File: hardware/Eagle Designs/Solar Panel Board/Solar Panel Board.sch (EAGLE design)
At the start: 34 parts, among them J1 MOLEX_503763-0291MOLEX_503763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, J2 MOLEX_503763-0491MOLEX_503763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

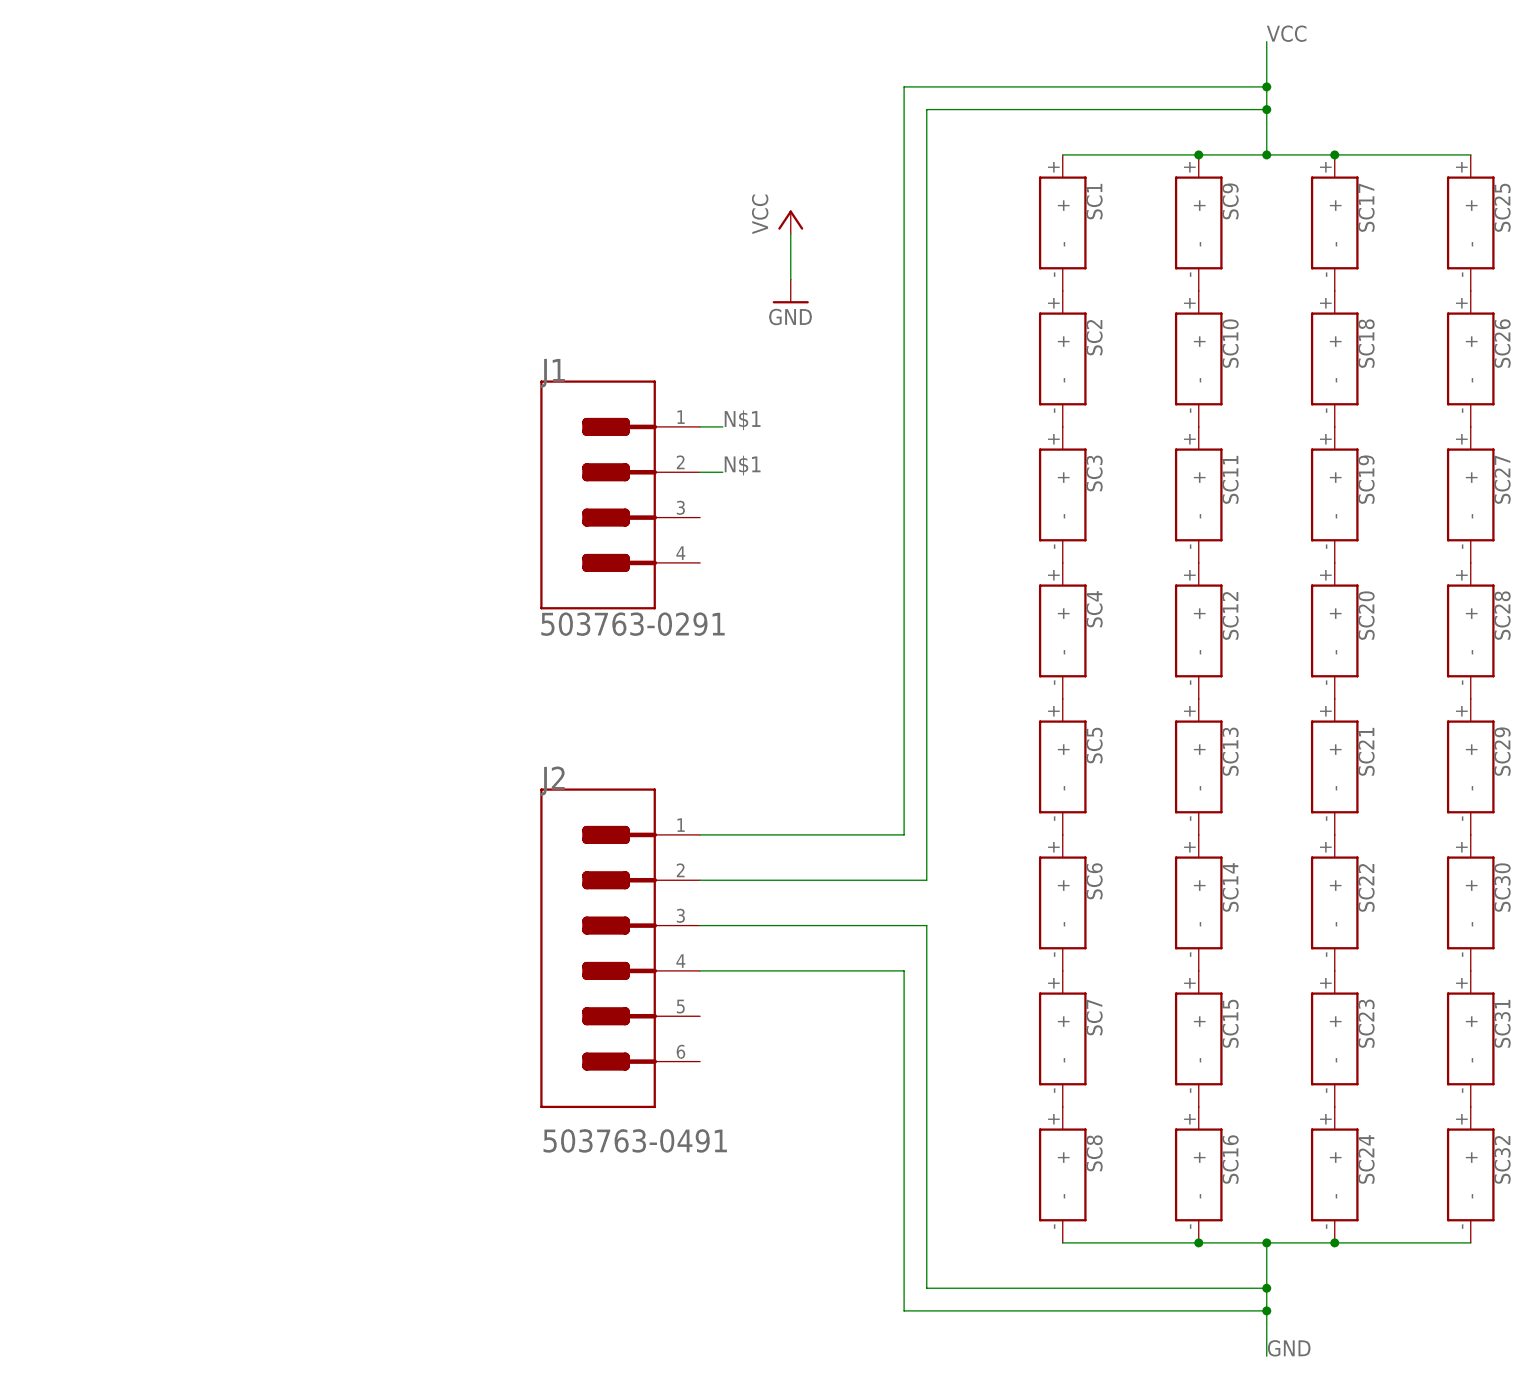
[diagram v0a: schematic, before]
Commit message: Moved solar panel boards to Eagle folder, deleted redudant OBC files
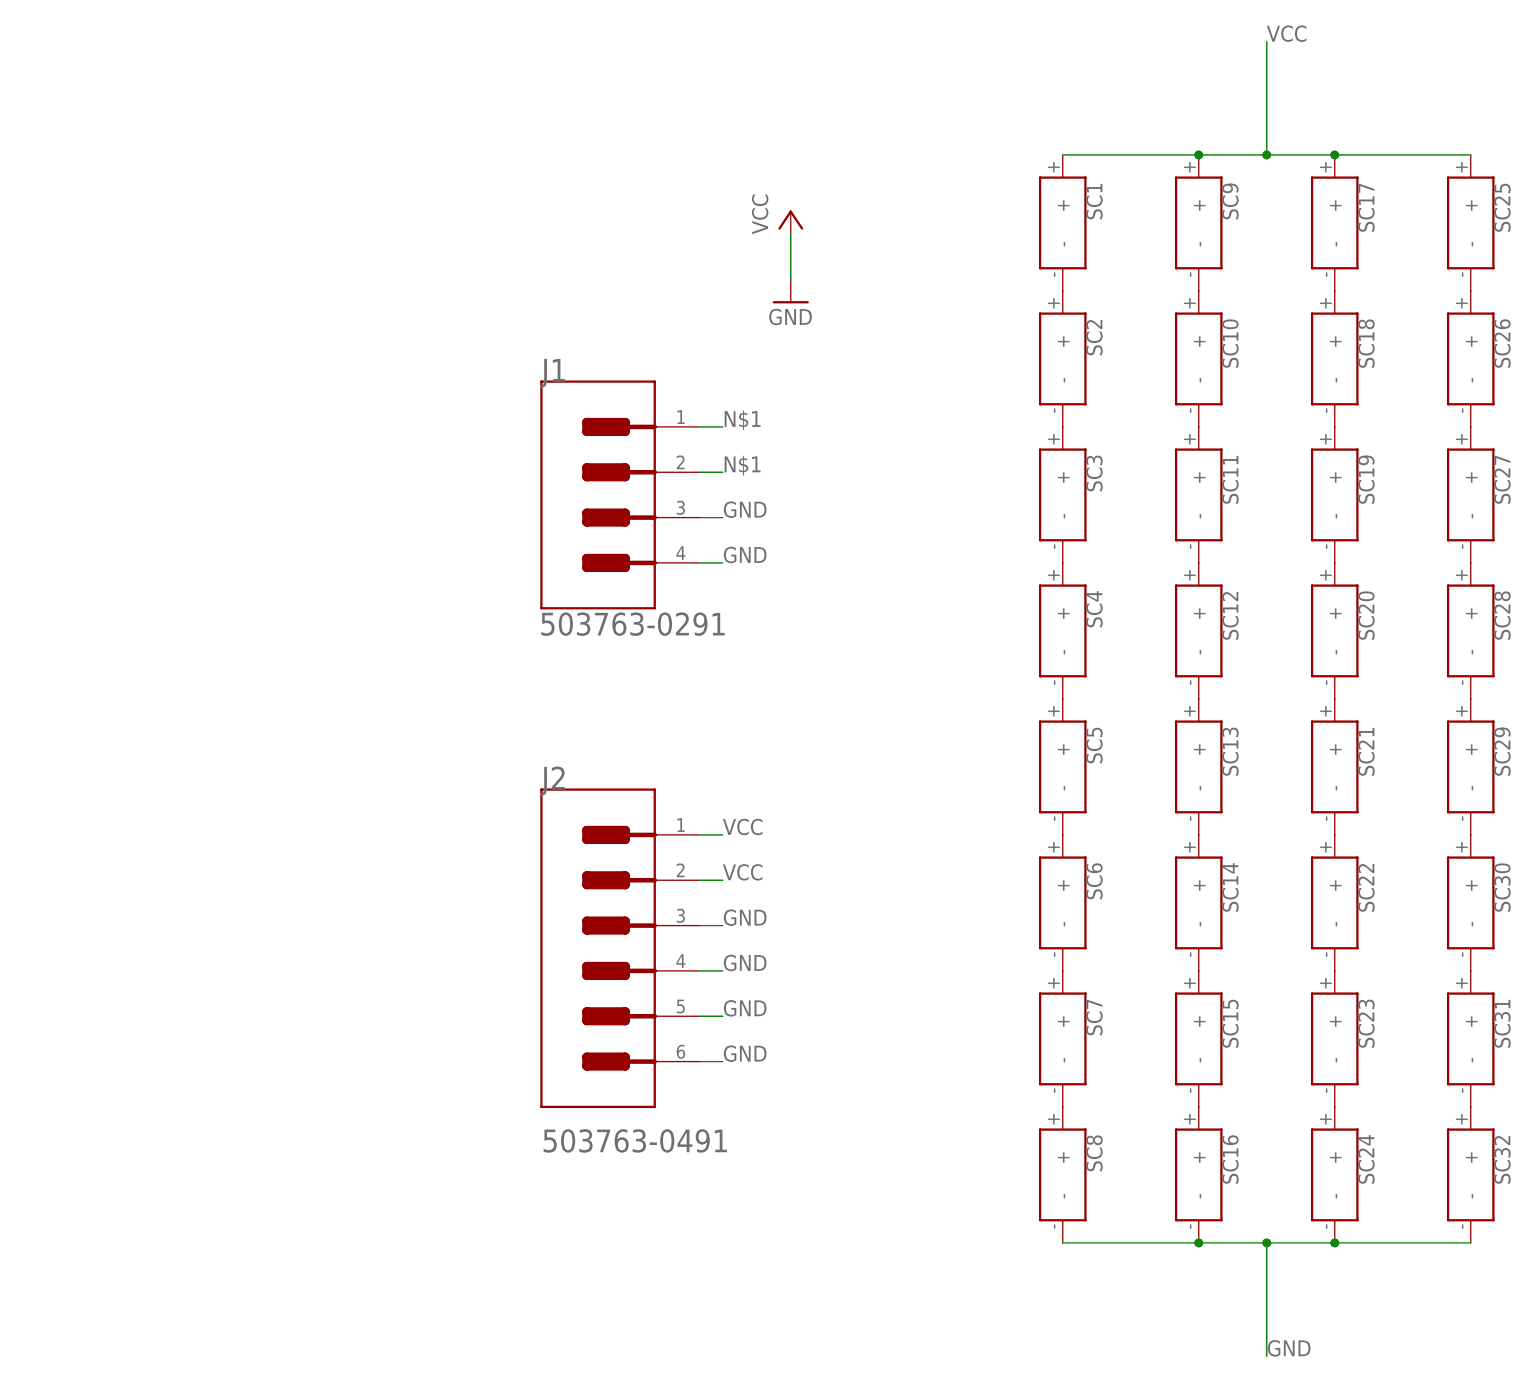
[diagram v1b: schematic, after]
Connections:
- net GND: now also J1.MNT_1, J1.MNT_2, J2.MNT_1, J2.MNT_2
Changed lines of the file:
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@@
 <segment>
 <pinref part="J2" gate="G$0" pin="1"/>
-<wire x1="416.56" y1="-33.02" x2="439.42" y2="-33.02" width="0.1524" layer="91"/>
-<wire x1="439.42" y1="-33.02" x2="439.42" y2="50.8" width="0.1524" layer="91"/>
+<wire x1="416.56" y1="-33.02" x2="419.1" y2="-33.02" width="0.1524" layer="91"/>
+<label x="419.1" y="-33.02" size="1.778" layer="95"/>
+</segment>
+<segment>
 <pinref part="SC25" gate="G$1" pin="+"/>
 <pinref part="SC17" gate="G$1" pin="+"/>
@@
 <junction x="487.68" y="43.18"/>
 <wire x1="480.06" y1="43.18" x2="487.68" y2="43.18" width="0.1524" layer="91"/>
-<wire x1="480.06" y1="43.18" x2="480.06" y2="48.26" width="0.1524" layer="91"/>
+<wire x1="480.06" y1="43.18" x2="480.06" y2="55.88" width="0.1524" layer="91"/>
 <junction x="480.06" y="43.18"/>
 <pinref part="SC9" gate="G$1" pin="+"/>
 <pinref part="SC1" gate="G$1" pin="+"/>
-<wire x1="480.06" y1="48.26" x2="480.06" y2="50.8" width="0.1524" layer="91"/>
-<wire x1="480.06" y1="50.8" x2="480.06" y2="55.88" width="0.1524" layer="91"/>
 <wire x1="457.2" y1="43.18" x2="472.44" y2="43.18" width="0.1524" layer="91"/>
 <wire x1="472.44" y1="43.18" x2="480.06" y2="43.18" width="0.1524" layer="91"/>
 <junction x="472.44" y="43.18"/>
 <label x="480.06" y="55.88" size="1.778" layer="95"/>
-<wire x1="439.42" y1="50.8" x2="480.06" y2="50.8" width="0.1524" layer="91"/>
-<junction x="480.06" y="50.8"/>
-<wire x1="441.96" y1="-38.1" x2="441.96" y2="48.26" width="0.1524" layer="91"/>
+</segment>
+<segment>
 <pinref part="J2" gate="G$0" pin="2"/>
-<wire x1="416.56" y1="-38.1" x2="441.96" y2="-38.1" width="0.1524" layer="91"/>
-<wire x1="441.96" y1="48.26" x2="480.06" y2="48.26" width="0.1524" layer="91"/>
-<junction x="480.06" y="48.26"/>
+<wire x1="416.56" y1="-38.1" x2="419.1" y2="-38.1" width="0.1524" layer="91"/>
+<label x="419.1" y="-38.1" size="1.778" layer="95"/>
 </segment>
 </net>
@@
 <segment>
 <pinref part="J2" gate="G$0" pin="4"/>
-<wire x1="416.56" y1="-48.26" x2="439.42" y2="-48.26" width="0.1524" layer="91"/>
-<wire x1="439.42" y1="-48.26" x2="439.42" y2="-86.36" width="0.1524" layer="91"/>
+<wire x1="416.56" y1="-48.26" x2="419.1" y2="-48.26" width="0.1524" layer="91"/>
+<label x="419.1" y="-48.26" size="1.778" layer="95"/>
+</segment>
+<segment>
+<pinref part="J1" gate="G$0" pin="MNT_1"/>
+<wire x1="416.56" y1="2.54" x2="419.1" y2="2.54" width="0.1524" layer="91"/>
+<label x="419.1" y="2.54" size="1.778" layer="95"/>
+</segment>
+<segment>
+<pinref part="J1" gate="G$0" pin="MNT_2"/>
+<wire x1="416.56" y1="-2.54" x2="419.1" y2="-2.54" width="0.1524" layer="91"/>
+<label x="419.1" y="-2.54" size="1.778" layer="95"/>
+</segment>
+<segment>
 <pinref part="SC32" gate="G$1" pin="-"/>
 <pinref part="SC24" gate="G$1" pin="-"/>
 <wire x1="487.68" y1="-78.74" x2="502.92" y2="-78.74" width="0.1524" layer="91"/>
 <junction x="487.68" y="-78.74"/>
+<wire x1="480.06" y1="-78.74" x2="487.68" y2="-78.74" width="0.1524" layer="91"/>
+<wire x1="480.06" y1="-78.74" x2="480.06" y2="-91.44" width="0.1524" layer="91"/>
+<junction x="480.06" y="-78.74"/>
 <pinref part="SC16" gate="G$1" pin="-"/>
 <junction x="472.44" y="-78.74"/>
 <wire x1="472.44" y1="-78.74" x2="480.06" y2="-78.74" width="0.1524" layer="91"/>
 <pinref part="SC8" gate="G$1" pin="-"/>
-<wire x1="480.06" y1="-78.74" x2="487.68" y2="-78.74" width="0.1524" layer="91"/>
 <wire x1="457.2" y1="-78.74" x2="472.44" y2="-78.74" width="0.1524" layer="91"/>
-<wire x1="480.06" y1="-78.74" x2="480.06" y2="-83.82" width="0.1524" layer="91"/>
-<junction x="480.06" y="-78.74"/>
 <label x="480.06" y="-91.44" size="1.778" layer="95"/>
+</segment>
+<segment>
+<pinref part="J2" gate="G$0" pin="MNT_2"/>
+<wire x1="416.56" y1="-58.42" x2="419.1" y2="-58.42" width="0.1524" layer="91"/>
+<label x="419.1" y="-58.42" size="1.778" layer="95"/>
+</segment>
+<segment>
+<pinref part="J2" gate="G$0" pin="MNT_1"/>
+<wire x1="416.56" y1="-53.34" x2="419.1" y2="-53.34" width="0.1524" layer="91"/>
+<label x="419.1" y="-53.34" size="1.778" layer="95"/>
+</segment>
+<segment>
 <pinref part="J2" gate="G$0" pin="3"/>
-<wire x1="480.06" y1="-83.82" x2="480.06" y2="-86.36" width="0.1524" layer="91"/>
-<wire x1="480.06" y1="-86.36" x2="480.06" y2="-91.44" width="0.1524" layer="91"/>
-<wire x1="416.56" y1="-43.18" x2="441.96" y2="-43.18" width="0.1524" layer="91"/>
-<wire x1="441.96" y1="-43.18" x2="441.96" y2="-83.82" width="0.1524" layer="91"/>
-<wire x1="441.96" y1="-83.82" x2="480.06" y2="-83.82" width="0.1524" layer="91"/>
-<junction x="480.06" y="-83.82"/>
-<wire x1="439.42" y1="-86.36" x2="480.06" y2="-86.36" width="0.1524" layer="91"/>
-<junction x="480.06" y="-86.36"/>
-</segment>
-</net>
+<wire x1="416.56" y1="-43.18" x2="419.1" y2="-43.18" width="0.1524" layer="91"/>
+<label x="419.1" y="-43.18" size="1.778" layer="95"/>
+</segment>
+</net>
